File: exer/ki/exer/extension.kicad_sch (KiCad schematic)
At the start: 17 parts, among them J1 Conn_01x20, J2 Conn_01x20, J3 Conn_01x34, J4 Conn_01x34, U10 74HCT574, U11 74HCT574, U12 74LS125, U13 74LS125, U14 74HCT574

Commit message: Correct schematics. Modify debugging. Fix copy/paste error where B inputs were set incorrectly. Add test vectors. Test vectors pass.
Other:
- note added: "PIN 35"
- note added: "PIN 44"
- note added: "PIN 49"
- note added: "PIN 53"
- note added: "PIN 68"
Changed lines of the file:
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@@
 	(wire
 		(pts
+			(xy 177.8 76.2) (xy 182.88 76.2)
+		)
+		(stroke
+			(width 0)
+			(type default)
+		)
+	)
+	(wire
+		(pts
 			(xy 93.98 198.12) (xy 93.98 185.42)
 		)
@@
 		)
 	)
+	(text "PIN 35"
+		(exclude_from_sim no)
+		(at 213.36 119.38 0)
+		(effects
+			(font
+				(size 1.27 1.27)
+			)
+		)
+	)
+	(text "PIN 68"
+		(exclude_from_sim no)
+		(at 213.36 35.56 0)
+		(effects
+			(font
+				(size 1.27 1.27)
+			)
+		)
+	)
 	(text "\"F\"\nPORT"
 		(exclude_from_sim no)
@@
 		)
 	)
+	(text "PIN 44"
+		(exclude_from_sim no)
+		(at 213.36 96.52 0)
+		(effects
+			(font
+				(size 1.27 1.27)
+			)
+		)
+	)
 	(text "\"A\"\nPORT"
 		(exclude_from_sim no)
@@
 		)
 	)
+	(text "PIN 49"
+		(exclude_from_sim no)
+		(at 213.36 83.82 0)
+		(effects
+			(font
+				(size 1.27 1.27)
+			)
+		)
+	)
+	(text "PIN 53"
+		(exclude_from_sim no)
+		(at 213.36 73.66 0)
+		(effects
+			(font
+				(size 1.27 1.27)
+			)
+		)
+	)
 	(label "B2_3"
 		(at 223.52 45.72 0)
@@
 	(global_label "TSTCLK"
 		(shape input)
-		(at 182.88 76.2 180)
+		(at 177.8 76.2 180)
 		(fields_autoplaced yes)
 		(effects
@@
 		)
 		(property "Intersheetrefs" "${INTERSHEET_REFS}"
-			(at 173.182 76.2 0)
+			(at 168.102 76.2 0)
 			(effects
 				(font

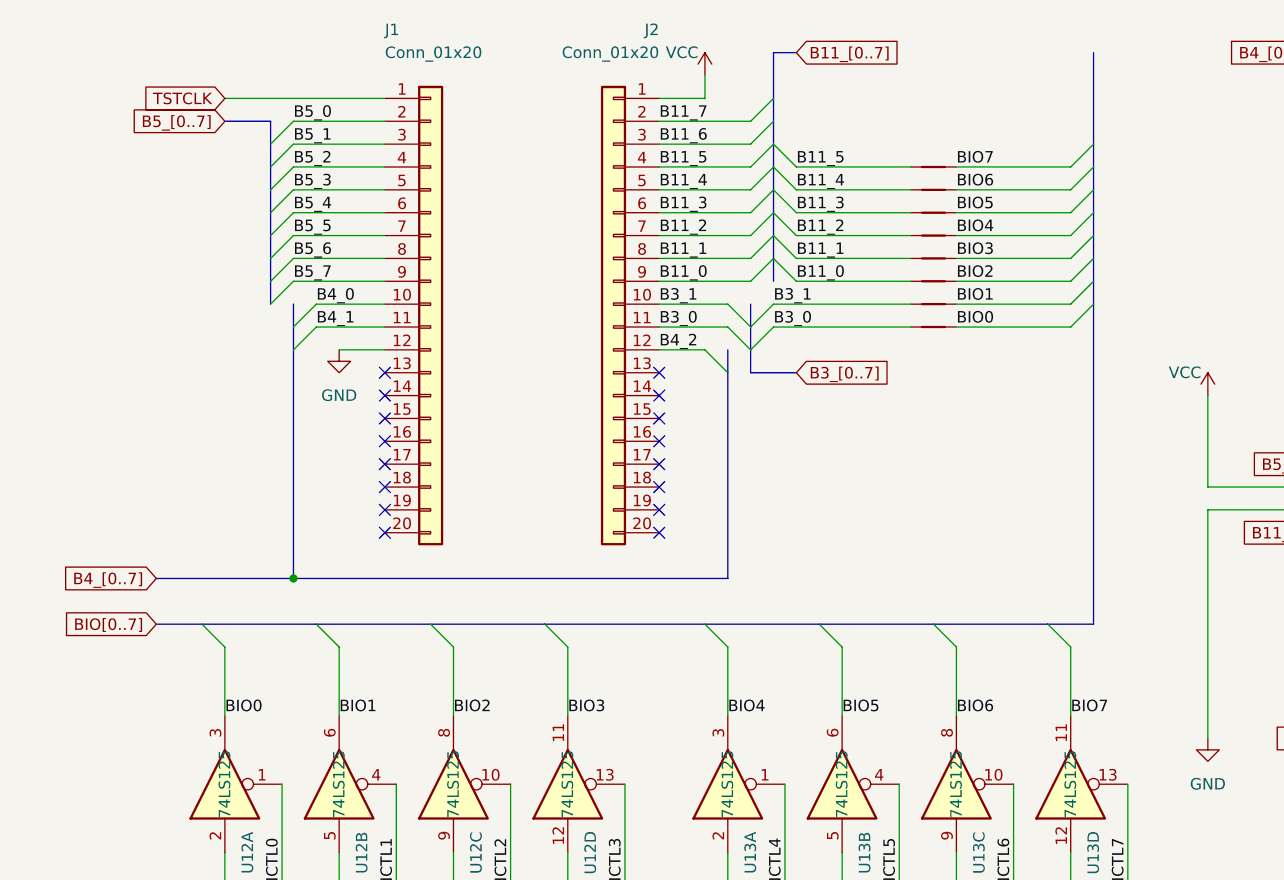
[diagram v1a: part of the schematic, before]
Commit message: Complete basic test vectors for L4C381. 4 units passed tests. Improve wiring for 24-pin ZIF socket. Also commit Fritzing changes in $YARC.
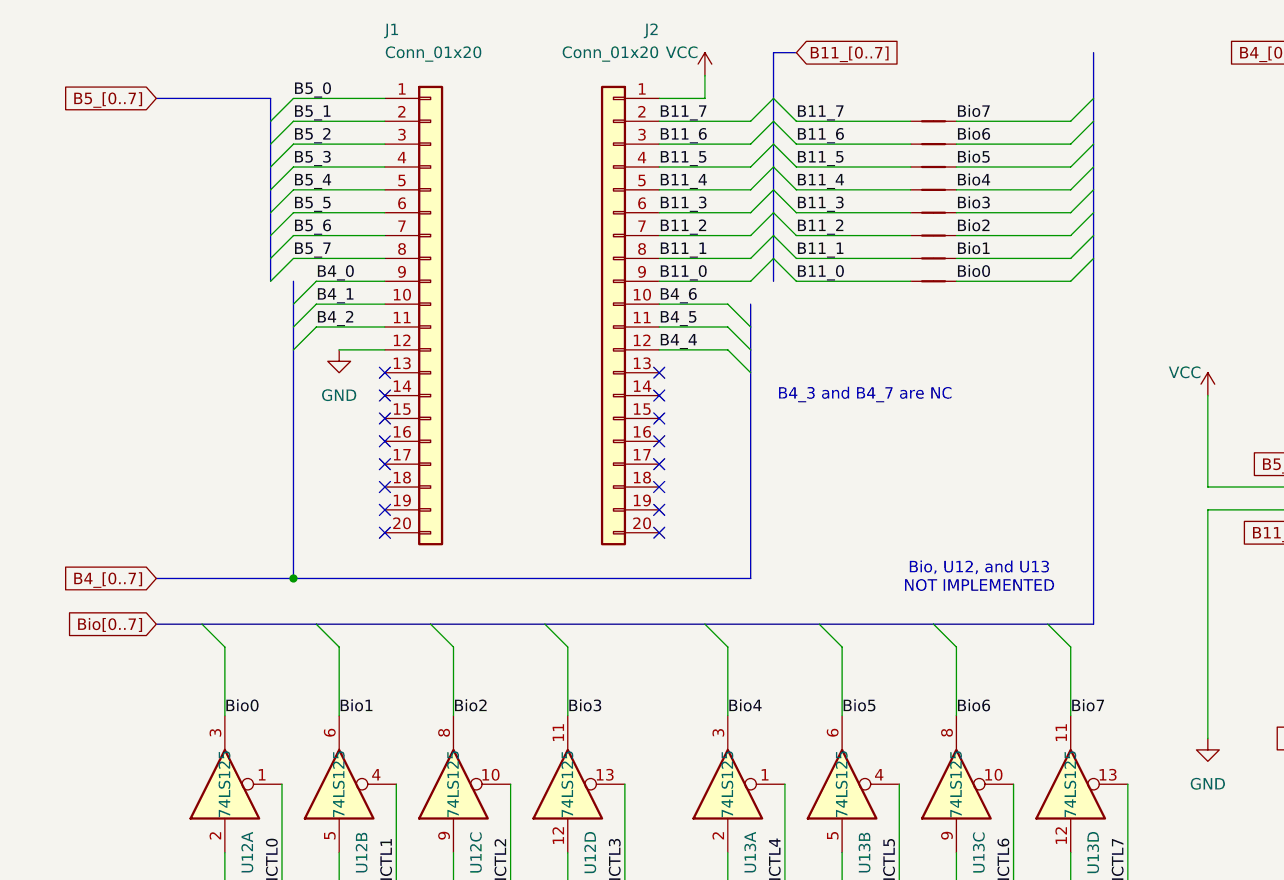
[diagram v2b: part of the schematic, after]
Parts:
- removed NT15, NT16: NetTie_2, symbol Device:NetTie_2
- added NT7, NT8: NetTie_2, symbol Device:NetTie_2
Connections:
- net B11_0: now also NT8.1; no longer NT6.1
- net B11_1: now also NT7.1; no longer NT5.1
- net B11_2: now also NT6.1; no longer NT4.1
- net B11_3: now also NT5.1; no longer NT3.1
- net B11_4: now also NT4.1; no longer NT2.1
- net B11_5: now also NT3.1; no longer NT1.1
- net B11_6: now also NT2.1
- net B11_7: now also NT1.1
- net B3_0: no longer J2.11 (Pin_11)
- net B3_1: no longer J2.10 (Pin_10)
- net B4_0: now also J1.9 (Pin_9); no longer J1.10 (Pin_10)
- net B4_1: now also J1.10 (Pin_10); no longer J1.11 (Pin_11)
- net B4_2: now also J1.11 (Pin_11); no longer J2.12 (Pin_12)
- net B4_4: now also J2.12 (Pin_12)
- net B4_5: now also J2.11 (Pin_11)
- net B4_6: now also J2.10 (Pin_10)
- net B5_0: now also J1.1 (Pin_1); no longer J1.2 (Pin_2)
- net B5_1: now also J1.2 (Pin_2); no longer J1.3 (Pin_3)
- net B5_2: now also J1.3 (Pin_3); no longer J1.4 (Pin_4)
- net B5_3: now also J1.4 (Pin_4); no longer J1.5 (Pin_5)
- net B5_4: now also J1.5 (Pin_5); no longer J1.6 (Pin_6)
- net B5_5: now also J1.6 (Pin_6); no longer J1.7 (Pin_7)
- net B5_6: now also J1.7 (Pin_7); no longer J1.8 (Pin_8)
- net B5_7: now also J1.8 (Pin_8); no longer J1.9 (Pin_9)
- net TSTCLK: no longer J1.1 (Pin_1)
- net BIO0 renamed Bio0
- net Bio0: now also NT8.2
- net BIO1 renamed Bio1
- net Bio1: now also NT7.2
- net BIO2 renamed Bio2
- net BIO3 renamed Bio3
- net BIO4 renamed Bio4
- net BIO5 renamed Bio5
- net BIO6 renamed Bio6
- net BIO7 renamed Bio7
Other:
- note added: "B4_3 and B4_7 are NC"
- note added: "Bio, U12, and U13 NOT IMPLEMENTED"
